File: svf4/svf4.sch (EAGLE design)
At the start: 79 parts, among them IC1 OPA4130P, IC2 OPA2134P, Q1 BC550B, Q10 2N3906, Q2 BC550B, Q3 2N3904, Q4 2N3904, Q5 2N3904, Q6 2N3904, Q7 2N3906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

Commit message: finished the rough draft of the state variable board
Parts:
- removed Q10, Q7, Q8, Q9: 2N3906, dan:2N3906
- removed Q3, Q4, Q5, Q6: 2N3904, dan:2N3904
- removed SV5, SV6: (no value), dan:MA04-1
- added C4, C5, C6: 4.7u, dan:CPOL-USE2.5-6
- added JP1, JP2: (no value), dan:PINHD-1X6
- added R32: 10k, dan:R-US_0207/2V
- added R33: 4.7k, dan:R-US_0207/2V
- added R34, R36: 1k, dan:R-US_0207/2V
- added R35: 100k, dan:R-US_0207/2V
- added U$1, U$2, U$3, U$4: 2N3904_, dan:2N3904_
- added U$5, U$6, U$7, U$8: 2N3906_, dan:2N3906_
- IC2: value OPA2134P -> OPA4130P; device dan:OPA2134P -> dan:OPA4130P
- R20: value 220k -> 1k
- R27: value 1k -> 4.7k
- R28: value 1k -> 3.3k
- R29: value 1k -> 100k
- R3: value 100k -> 82k
- R30, R31: value 10k -> 100k
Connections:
- new net N$38: BPOUT.P$3, R34.2, R35.1
- new net N$41: IC2D.OUT, R32.2, SV7.4
- new net N$42: IC2D.-IN, R32.1, R33.2
- new net N$43: C6.-, R27.1
- new net N$44: C5.+, R26.1
- new net N$45: C4.-, R34.1
- new net N$46: JP2.4, R31.2
- new net N$47: IC2B.+IN, R20.1
- new net N$48: IC2B.-IN, R36.2
- net +12V: now also IC2A.V+; no longer IC2P.V+
- net -12V: now also IC2A.V-; no longer IC2P.V-
- net -1V: now also IC2C.+IN; no longer IC2B.+IN
- net BP: now also JP2.6; no longer SV5.1
- net GND: now also JP1.2, JP1.5, JP2.2, JP2.5, R20.2, R33.1, R35.2, U$2.B, U$4.B; no longer Q4.B, Q6.B, SV5.2, SV6.2
- net HP: now also IC2D.+IN; no longer SV7.4
- net IN: now also IC1A.-IN, R24.2, R30.1, R31.1, R5.2, R6.2; no longer R20.2, SV5.3
- net N$1: now also U$3.E, U$4.E; no longer Q5.E, Q6.E
- net N$10: now also U$4.C, U$8.C; no longer Q10.C, Q6.C
- net N$14: now also U$3.C, U$7.B, U$7.C, U$8.B; no longer Q10.B, Q5.C, Q9.B, Q9.C
- net N$15: now also U$3.B; no longer Q5.B
- net N$16: now also JP2.1; no longer SV5.4
- net N$17: now also U$7.E, U$8.E; no longer Q10.E, Q9.E
- net N$2: now also U$2.C, U$6.C; no longer Q4.C, Q8.C
- net N$26: now also IC2C.OUT; no longer IC2B.OUT
- net N$28: now also IC2C.-IN; no longer IC2B.-IN
- net N$3: now also U$5.E, U$6.E; no longer Q7.E, Q8.E
- net N$30: now also JP1.1; no longer SV6.4
- net N$32: now also C5.-; no longer R26.1
- net N$33: now also JP1.4; no longer R30.2
- net N$36: now also C4.+, JP1.6; no longer BPOUT.P$3, SV6.1
- net N$37: now also JP2.3, R30.2; no longer R30.1, R31.1, SV6.3
- net N$4: now also U$1.C, U$5.B, U$5.C, U$6.B; no longer Q3.C, Q7.B, Q7.C, Q8.B
- net N$40: now also JP1.3; no longer R31.2
- net N$5: now also U$1.E, U$2.E; no longer Q3.E, Q4.E
- net N$6: now also U$1.B; no longer Q3.B
- net N$7: now also IC2B.OUT, R36.1; no longer IC1A.-IN, R20.1, R24.2, R5.2, R6.2
- net N$8: now also C6.+; no longer R27.1
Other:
- note removed: "attenuated inputs to otas more"
- note removed: "reduced attenuation of input"
- note removed: "reduced capacitor size to account"
- note removed: "reduced feedback from lp out to input"
- note removed: "self oscillating version:"
- moved on the sheet: IC2B, R20, R27, R28, R30, R31

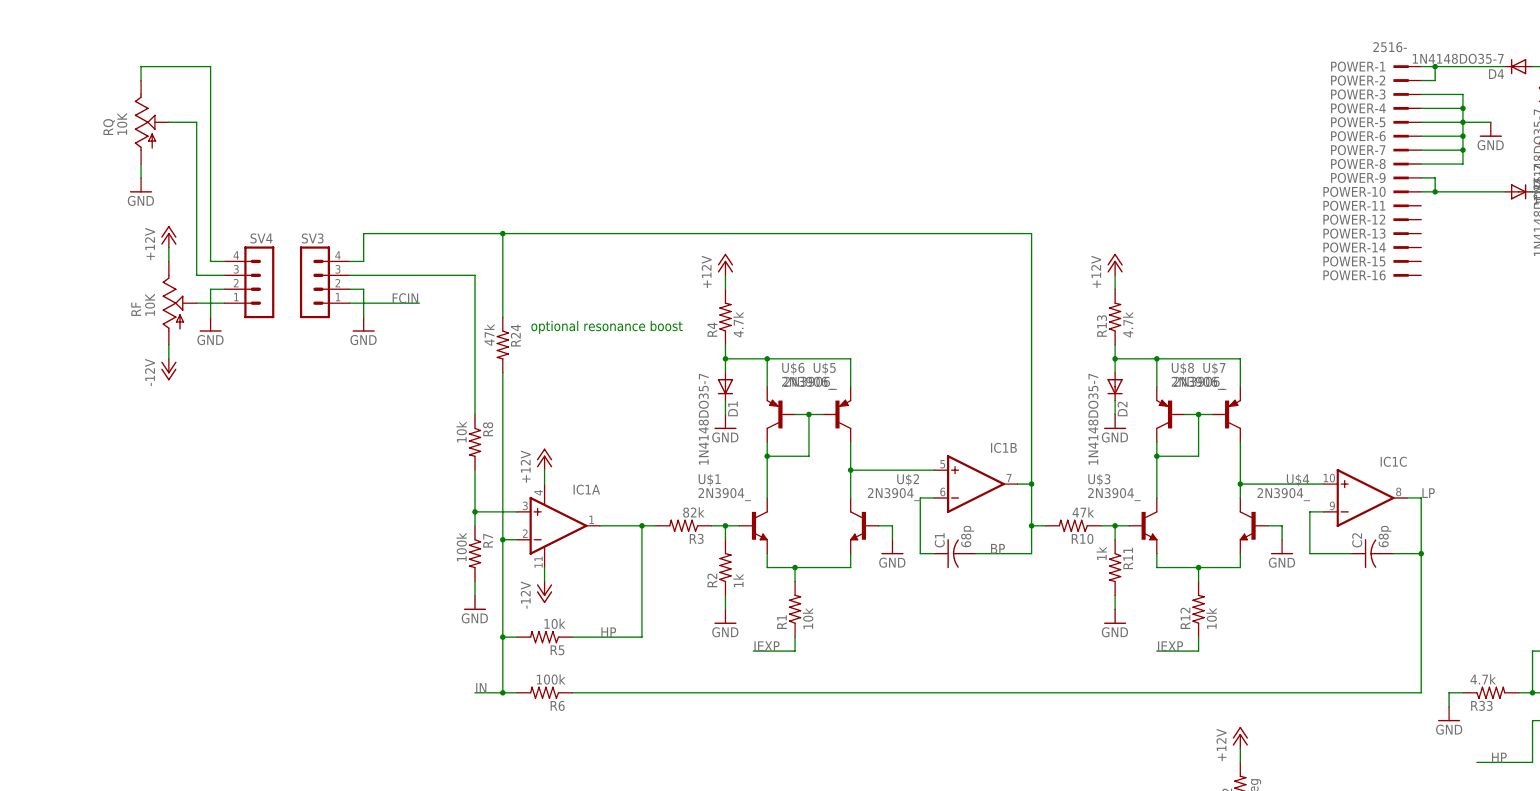
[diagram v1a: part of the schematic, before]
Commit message: sent svf to fab.  fixed some significatn errors
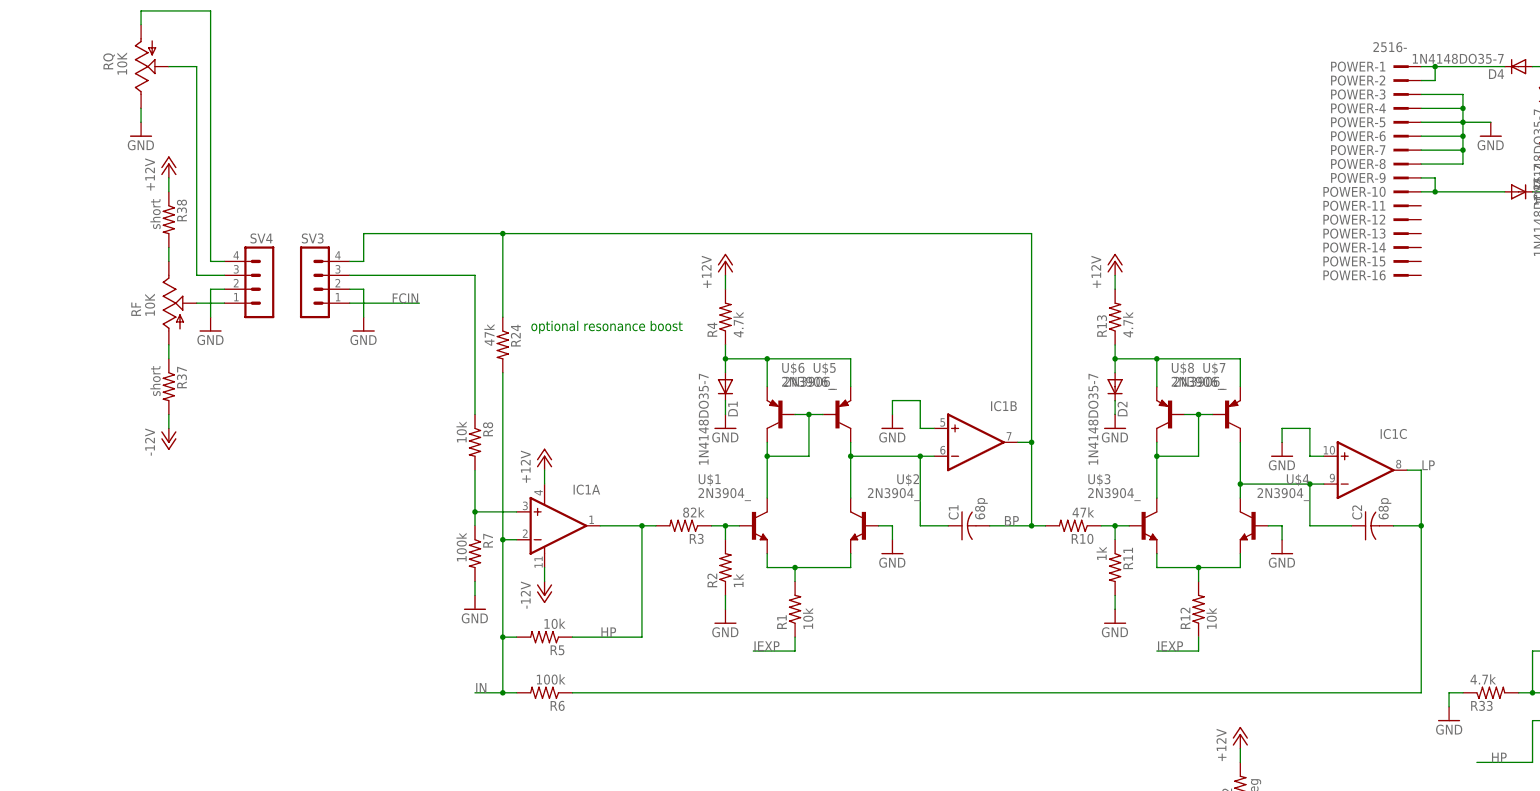
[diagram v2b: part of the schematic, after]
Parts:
- added R37, R38: short, dan:R-US_0204/7
- R18, R26, R27, R28, R29, R34, R35: device dan:R-US_0207/2V -> dan:R-US_0204/7
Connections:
- removed net N$10: IC1C.+IN, U$4.C, U$8.C
- removed net N$2: IC1B.+IN, U$2.C, U$6.C
- new net N$49: R38.2, RF.E
- new net N$50: R37.1, RF.A
- net +12V: now also R38.1; no longer RF.E
- net -12V: now also R37.2; no longer RF.A
- net GND: now also IC1B.+IN, IC1C.+IN, RQ.E; no longer RQ.A
- net N$11: now also U$2.C, U$6.C
- net N$18: now also U$4.C, U$8.C
- net N$25: now also RQ.A; no longer RQ.E
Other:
- moved on the sheet: C1, C2, IC1B, IC1C, RQ

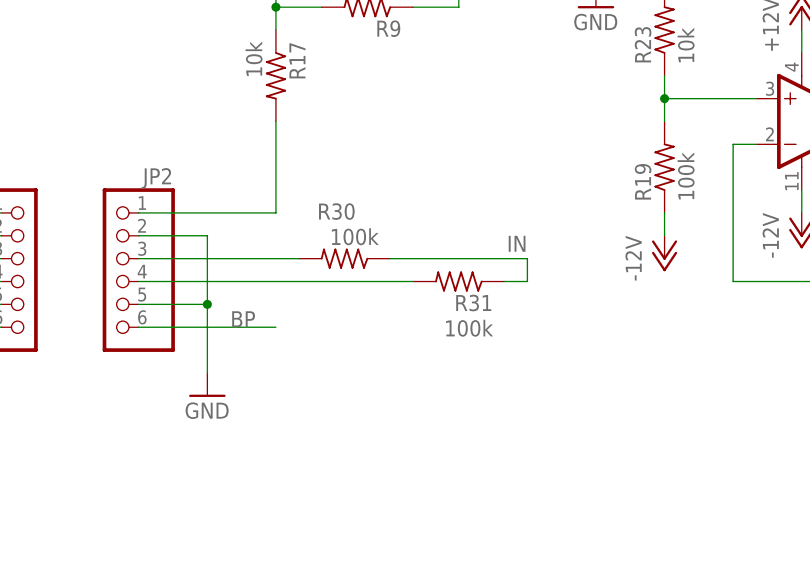
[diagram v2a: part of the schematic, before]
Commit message: respun the svf.  changed a few components on the 3320
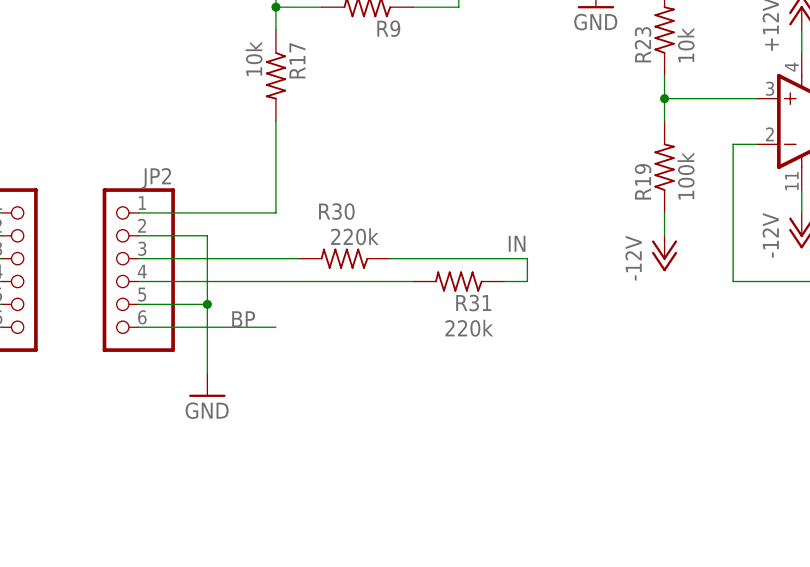
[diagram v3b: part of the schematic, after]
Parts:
- R30, R31: value 100k -> 220k
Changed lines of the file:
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@@
 <part name="JP1" library="dan" deviceset="PINHD-1X6" device=""/>
 <part name="JP2" library="dan" deviceset="PINHD-1X6" device=""/>
-<part name="R30" library="dan" deviceset="R-US_" device="0207/2V" value="100k"/>
-<part name="R31" library="dan" deviceset="R-US_" device="0207/2V" value="100k"/>
+<part name="R30" library="dan" deviceset="R-US_" device="0207/2V" value="220k"/>
+<part name="R31" library="dan" deviceset="R-US_" device="0207/2V" value="220k"/>
 <part name="GND33" library="dan" deviceset="GND" device=""/>
 <part name="R20" library="dan" deviceset="R-US_" device="0207/2V" value="1k"/>

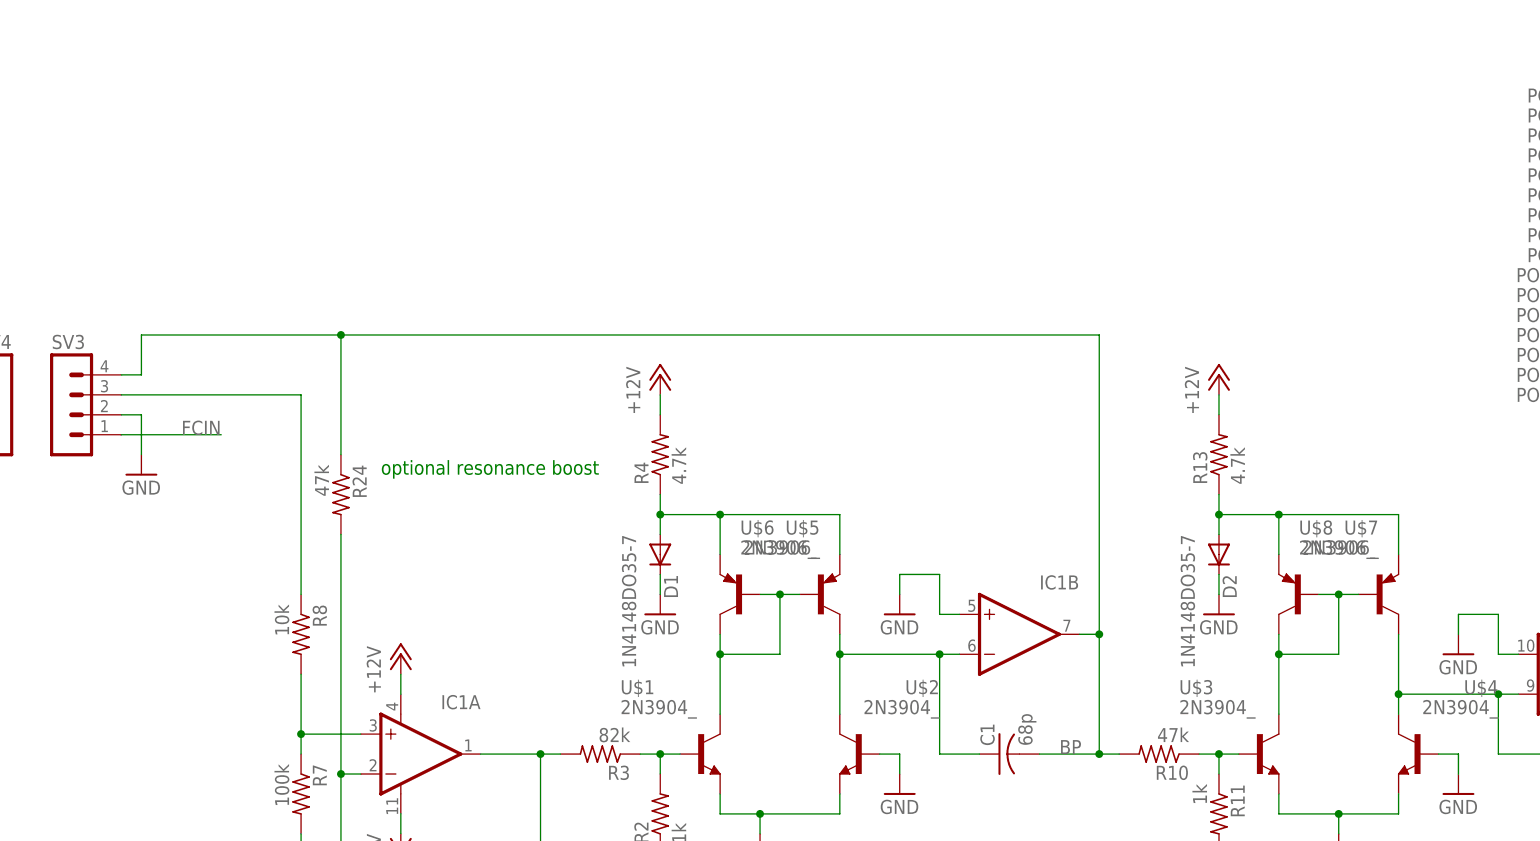
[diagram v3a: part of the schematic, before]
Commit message: updated svf with dc offset trim pots and transistors for biasing
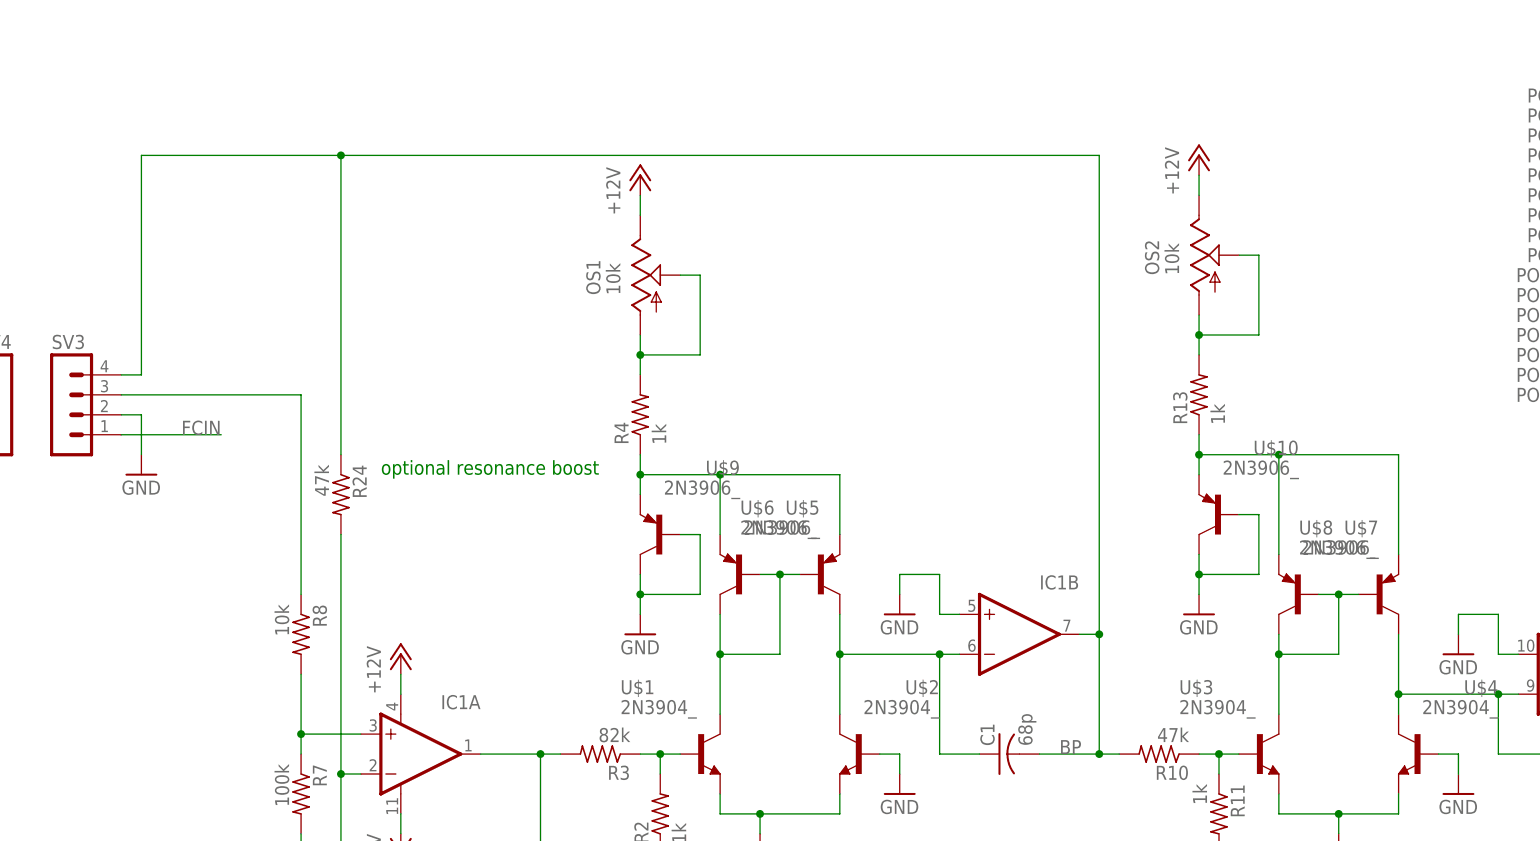
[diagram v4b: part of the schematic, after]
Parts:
- removed D1, D2: 1N4148DO35-7, dan:1N4148DO35-7
- added OS1, OS2: 10k, dan:TRIM_US-S64W
- added U$10, U$9: 2N3906_, dan:2N3906_
- R13, R4: value 4.7k -> 1k
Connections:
- new net N$10: OS2.A, OS2.S, R13.2
- new net N$2: OS1.A, OS1.S, R4.2
- net +12V: now also OS1.E, OS2.E; no longer R13.2, R4.2
- net GND: now also U$10.B, U$10.C, U$9.B, U$9.C; no longer D1.C, D2.C
- net N$17: now also U$10.E; no longer D2.A
- net N$3: now also U$9.E; no longer D1.A
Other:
- moved on the sheet: R13, R4, U$5, U$6
